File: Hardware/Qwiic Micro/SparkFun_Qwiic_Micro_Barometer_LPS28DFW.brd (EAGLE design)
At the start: 7.6 x 19.1 mm, 38 parts, among them J2 QWIIC_RIGHT_ANGLE, U1 LPS28DFW

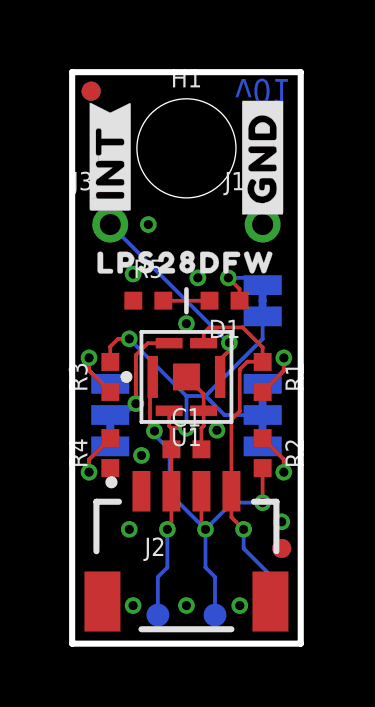
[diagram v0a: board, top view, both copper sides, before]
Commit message: Update Micro with mirrored LPS28DFW footprint
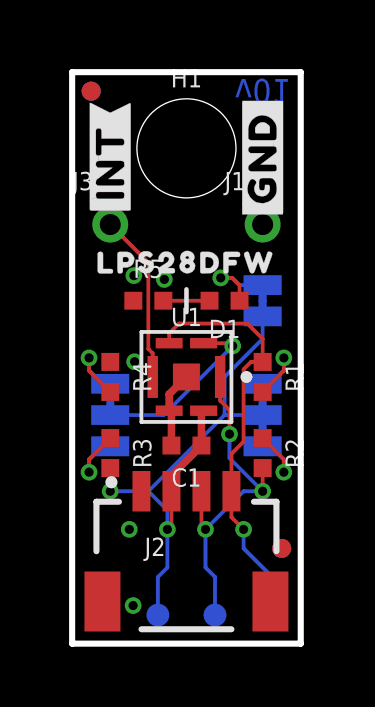
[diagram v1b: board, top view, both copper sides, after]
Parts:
- moved R3 2.54 mm to (1.27, 6.35), turned to 270 degrees
- moved R4 2.54 mm to (1.27, 8.89), turned to 270 degrees
- moved C1 0.13 mm to (3.81, 6.60), turned to 180 degrees
- turned ADR to 90 degrees
- turned U1 to 0 degrees
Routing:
- net ADR: track 3.90 -> 6.04 mm
- net SDA: track 13.6 -> 11.9 mm
- net SCL: track 12.9 -> 14.2 mm
- net INT: track 6.87 -> 5.67 mm, vias 1 -> 0
- net N$4: track 2.16 -> 2.74 mm
- net 3.3V: track 19.3 -> 19.7 mm, vias 3 -> 2
- net GND: track 2.71 -> 2.56 mm, vias 11 -> 5

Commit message: Design review updates
Add silk to PWR LED on 1x1
Tweak routing to use more T-junctions and route into side of pads rather than corners
Move via on I2C jumper silk of Micro
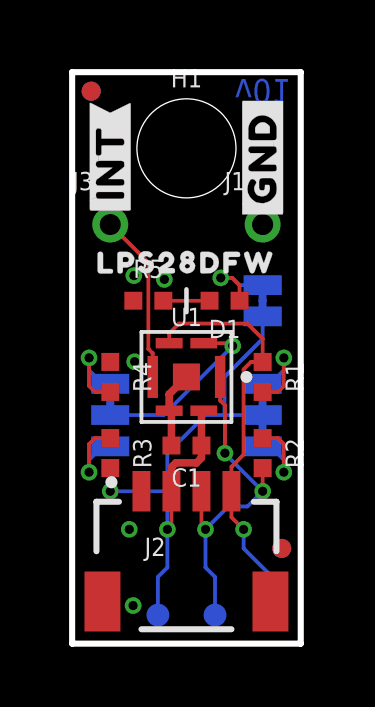
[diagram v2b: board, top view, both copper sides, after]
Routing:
- net 3.3V: track 19.7 -> 20.6 mm
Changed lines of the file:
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@@
 <wire x1="3.175" y1="2.54" x2="2.8575" y2="2.2225" width="0.127" layer="16"/>
 <wire x1="2.8575" y1="2.2225" x2="2.8575" y2="0.9525" width="0.127" layer="16"/>
-<wire x1="3.31" y1="5.08" x2="3.31" y2="5.604" width="0.254" layer="1"/>
-<wire x1="3.31" y1="5.604" x2="4.31" y2="6.604" width="0.254" layer="1"/>
 <wire x1="4.31" y1="6.604" x2="4.31" y2="7.69" width="0.254" layer="1"/>
 <wire x1="4.31" y1="7.69" x2="4.385" y2="7.765" width="0.254" layer="1"/>
@@
 <wire x1="5.08" y1="8.89" x2="6.35" y2="10.16" width="0.127" layer="16"/>
 <wire x1="6.35" y1="10.16" x2="6.35" y2="10.9093" width="0.127" layer="16"/>
-<wire x1="3.175" y1="3.81" x2="3.175" y2="4.445" width="0.127" layer="16"/>
-<wire x1="3.175" y1="4.445" x2="2.54" y2="5.08" width="0.127" layer="16"/>
-<wire x1="1.27" y1="5.08" x2="2.54" y2="5.08" width="0.127" layer="16"/>
+<wire x1="3.175" y1="3.81" x2="3.175" y2="5.08" width="0.127" layer="16"/>
+<wire x1="3.175" y1="5.08" x2="3.175" y2="6.35" width="0.127" layer="16"/>
+<wire x1="1.27" y1="5.08" x2="3.175" y2="5.08" width="0.127" layer="16"/>
 <via x="1.27" y="5.08" extent="1-16" drill="0.3048"/>
 <wire x1="1.27" y1="5.08" x2="1.27" y2="5.85" width="0.127" layer="1"/>
-<wire x1="2.54" y1="5.08" x2="5.08" y2="7.62" width="0.127" layer="16"/>
+<wire x1="3.175" y1="6.35" x2="4.445" y2="7.62" width="0.127" layer="16"/>
+<wire x1="3.31" y1="5.08" x2="3.31" y2="5.8802" width="0.254" layer="1"/>
+<wire x1="3.31" y1="5.8802" x2="3.4544" y2="6.0246" width="0.254" layer="1"/>
+<wire x1="3.4544" y1="6.0246" x2="4.145" y2="6.0246" width="0.254" layer="1"/>
+<wire x1="4.31" y1="6.1896" x2="4.31" y2="6.604" width="0.254" layer="1"/>
+<wire x1="4.145" y1="6.0246" x2="4.31" y2="6.1896" width="0.254" layer="1"/>
+<wire x1="5.08" y1="7.62" x2="4.445" y2="7.62" width="0.127" layer="16"/>
 </signal>
 <signal name="SDA">
@@
 <wire x1="4.7625" y1="2.2225" x2="4.7625" y2="0.9525" width="0.127" layer="16"/>
 <wire x1="4.7625" y1="2.2225" x2="4.445" y2="2.54" width="0.127" layer="16"/>
-<wire x1="4.445" y1="3.81" x2="5.715" y2="5.08" width="0.127" layer="16"/>
-<wire x1="5.715" y1="5.08" x2="6.35" y2="5.08" width="0.127" layer="16"/>
+<wire x1="4.445" y1="3.81" x2="5.207" y2="4.572" width="0.127" layer="16"/>
+<wire x1="5.842" y1="4.572" x2="5.207" y2="4.572" width="0.127" layer="16"/>
+<wire x1="5.842" y1="4.572" x2="6.35" y2="5.08" width="0.127" layer="16"/>
 <via x="6.35" y="5.08" extent="1-16" drill="0.3048"/>
 <wire x1="6.35" y1="5.08" x2="6.35" y2="5.85" width="0.127" layer="1"/>
 <wire x1="4.935" y1="8.89" x2="4.935" y2="8.1026" width="0.127" layer="1"/>
-<wire x1="5.2451" y1="7.7925" x2="4.935" y2="8.1026" width="0.127" layer="1"/>
-<wire x1="5.2451" y1="7.7925" x2="5.2451" y2="6.985" width="0.127" layer="1"/>
-<via x="5.2451" y="6.985" extent="1-16" drill="0.3048"/>
-<wire x1="5.2451" y1="6.985" x2="5.2451" y2="6.1849" width="0.127" layer="16"/>
-<wire x1="5.2451" y1="6.1849" x2="6.35" y2="5.08" width="0.127" layer="16"/>
+<wire x1="5.0927" y1="7.9449" x2="4.935" y2="8.1026" width="0.127" layer="1"/>
+<wire x1="5.0927" y1="7.9449" x2="5.0927" y2="6.35" width="0.127" layer="1"/>
+<via x="5.0927" y="6.35" extent="1-16" drill="0.3048"/>
+<wire x1="5.0927" y1="6.35" x2="5.0927" y2="6.3373" width="0.127" layer="16"/>
+<wire x1="5.0927" y1="6.3373" x2="6.35" y2="5.08" width="0.127" layer="16"/>
 </signal>
 <signal name="SCL">
@@
 <wire x1="6.6675" y1="2.2225" x2="6.6675" y2="0.9525" width="0.127" layer="16"/>
 <wire x1="6.6675" y1="2.2225" x2="5.715" y2="3.175" width="0.127" layer="16"/>
-<wire x1="5.31" y1="5.08" x2="5.31" y2="6.326" width="0.127" layer="1"/>
-<wire x1="5.715" y1="6.731" x2="5.715" y2="9.144" width="0.127" layer="1"/>
+<wire x1="5.31" y1="5.08" x2="5.31" y2="5.8942" width="0.127" layer="1"/>
+<wire x1="5.715" y1="6.2992" x2="5.715" y2="9.144" width="0.127" layer="1"/>
 <wire x1="5.715" y1="9.144" x2="5.961" y2="9.39" width="0.127" layer="1"/>
 <wire x1="5.961" y1="9.39" x2="6.35" y2="9.39" width="0.127" layer="1"/>
-<wire x1="5.31" y1="6.326" x2="5.715" y2="6.731" width="0.127" layer="1"/>
+<wire x1="5.31" y1="5.8942" x2="5.715" y2="6.2992" width="0.127" layer="1"/>
 <wire x1="6.35" y1="9.39" x2="6.35" y2="10.16" width="0.127" layer="1"/>
 <wire x1="6.35" y1="10.16" x2="5.842" y2="10.668" width="0.127" layer="1"/>
@@
 <contactref element="R1" pad="2"/>
 <contactref element="I2C" pad="3"/>
-<wire x1="6.35" y1="8.39" x2="7.0564" y2="9.0964" width="0.127" layer="1"/>
-<wire x1="7.0564" y1="9.0964" x2="7.0564" y2="9.525" width="0.127" layer="1"/>
+<wire x1="7.0564" y1="8.5884" x2="6.858" y2="8.39" width="0.127" layer="1"/>
+<wire x1="6.35" y1="8.39" x2="6.858" y2="8.39" width="0.127" layer="1"/>
+<wire x1="7.0564" y1="8.5884" x2="7.0564" y2="9.525" width="0.127" layer="1"/>
 <via x="7.0564" y="9.525" extent="1-16" drill="0.3048"/>
 <wire x1="7.0564" y1="9.525" x2="7.0564" y2="9.1138" width="0.127" layer="16"/>
@@
 <contactref element="R2" pad="1"/>
 <contactref element="I2C" pad="1"/>
-<wire x1="6.35" y1="6.85" x2="7.0564" y2="6.1436" width="0.127" layer="1"/>
-<wire x1="7.0564" y1="6.1436" x2="7.0564" y2="5.715" width="0.127" layer="1"/>
+<wire x1="7.0564" y1="6.6516" x2="6.858" y2="6.85" width="0.127" layer="1"/>
+<wire x1="6.35" y1="6.85" x2="6.858" y2="6.85" width="0.127" layer="1"/>
+<wire x1="7.0564" y1="6.6516" x2="7.0564" y2="5.715" width="0.127" layer="1"/>
 <via x="7.0564" y="5.715" extent="1-16" drill="0.3048"/>
 <wire x1="7.0564" y1="5.715" x2="7.0564" y2="6.1262" width="0.127" layer="16"/>
@@
 <contactref element="R4" pad="2"/>
 <contactref element="ADR" pad="3"/>
-<wire x1="1.27" y1="8.39" x2="0.5636" y2="9.0964" width="0.127" layer="1"/>
-<wire x1="0.5636" y1="9.0964" x2="0.5636" y2="9.525" width="0.127" layer="1"/>
+<wire x1="1.27" y1="8.39" x2="0.762" y2="8.39" width="0.127" layer="1"/>
+<wire x1="0.762" y1="8.39" x2="0.5636" y2="8.5884" width="0.127" layer="1"/>
+<wire x1="0.5636" y1="8.5884" x2="0.5636" y2="9.525" width="0.127" layer="1"/>
 <via x="0.5636" y="9.525" extent="1-16" drill="0.3048"/>
 <wire x1="0.5636" y1="9.525" x2="0.5636" y2="9.1138" width="0.127" layer="16"/>
@@
 <contactref element="ADR" pad="1"/>
 <contactref element="R3" pad="1"/>
-<wire x1="1.27" y1="6.85" x2="0.5636" y2="6.1436" width="0.127" layer="1"/>
-<wire x1="0.5636" y1="6.1436" x2="0.5636" y2="5.715" width="0.127" layer="1"/>
+<wire x1="1.27" y1="6.85" x2="0.762" y2="6.85" width="0.127" layer="1"/>
+<wire x1="0.762" y1="6.85" x2="0.5636" y2="6.6516" width="0.127" layer="1"/>
+<wire x1="0.5636" y1="6.6516" x2="0.5636" y2="5.715" width="0.127" layer="1"/>
 <via x="0.5636" y="5.715" extent="1-16" drill="0.3048"/>
 <wire x1="0.5636" y1="5.715" x2="0.5636" y2="6.1262" width="0.127" layer="16"/>
